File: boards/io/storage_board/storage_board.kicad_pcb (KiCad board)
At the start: 2 copper layers, 40.6 x 20.3 mm, 17 parts, among them J1 Conn_02x06_Top_Bottom, J2 Conn_02x02_Odd_Even, Q1 2SC3325, Q2 2SC3325, Q3 2SC3325, Q4 2SC3325, U1 24FC512

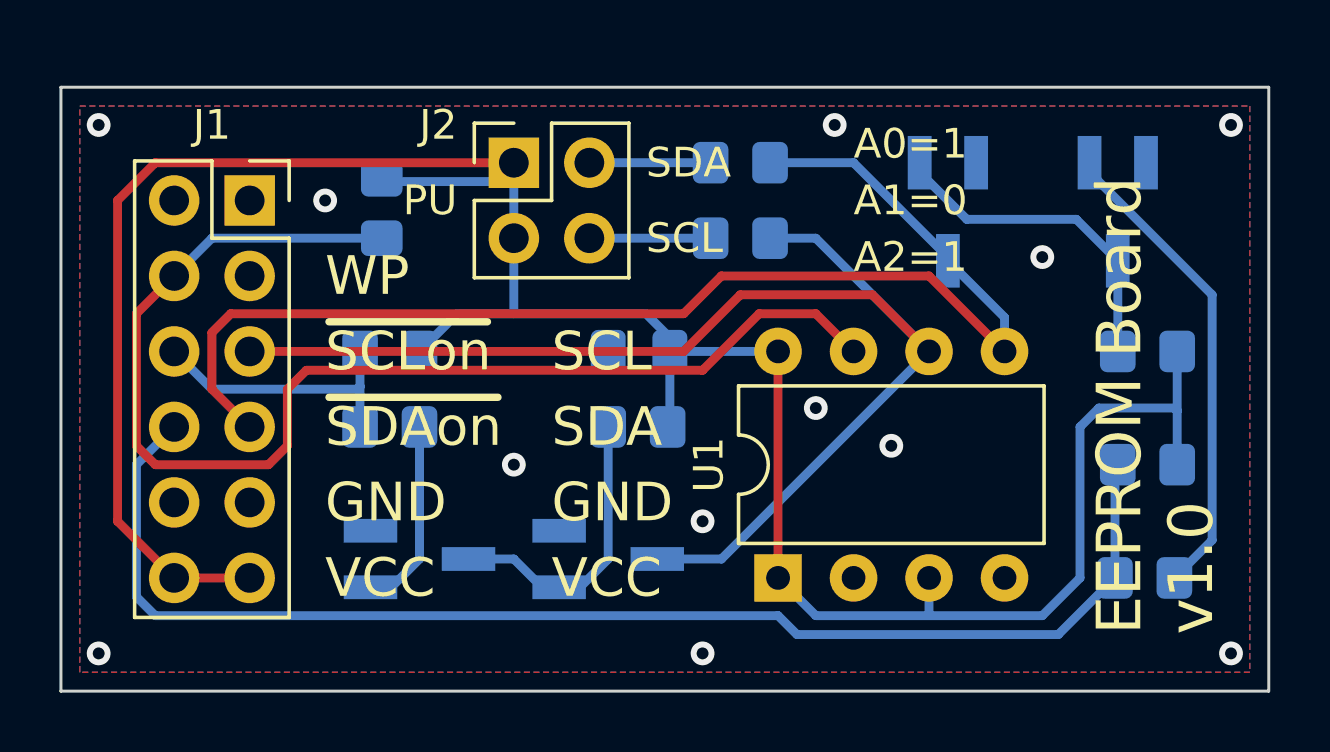
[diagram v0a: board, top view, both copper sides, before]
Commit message: storage_board: rename and improve line width
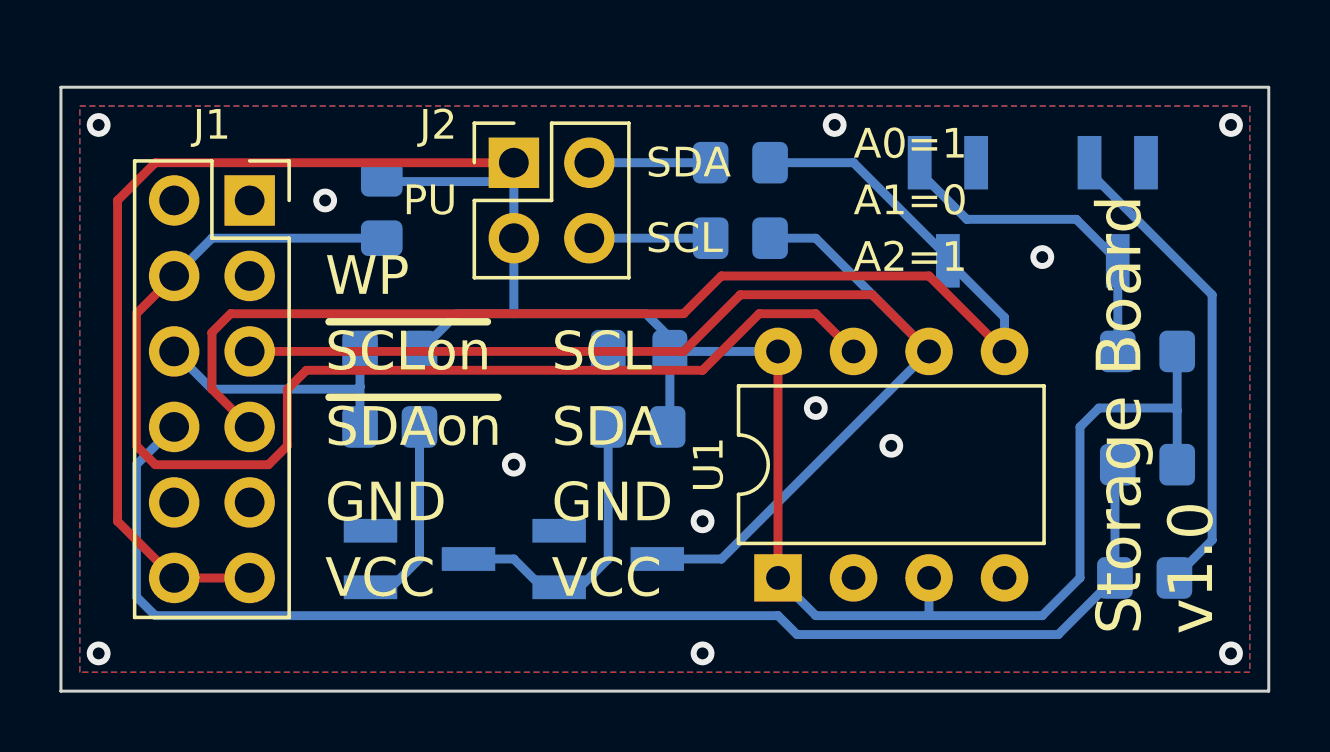
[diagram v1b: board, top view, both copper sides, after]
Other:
- board text added: "Storage Board v1.0"
- board text removed: "EEPROM Board v1.0"

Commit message: release boards
* rom_adapter_for_nucky
* software_rom2
* eprom_zps
* convenient_port_shield
* storage_board
* timer_board
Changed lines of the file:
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@@
     (aux_axis_origin 85.09 87.63)
     (pcbplotparams
-      (layerselection 0x00010fc_ffffffff)
+      (layerselection 0x00010f0_ffffffff)
       (disableapertmacros false)
       (usegerberextensions false)
@@
       (viasonmask false)
       (mode 1)
-      (useauxorigin false)
+      (useauxorigin true)
       (hpglpennumber 1)
       (hpglpenspeed 20)
@@
       (outputformat 1)
       (mirror false)
-      (drillshape 1)
+      (drillshape 0)
       (scaleselection 1)
-      (outputdirectory "")
+      (outputdirectory "../../../../release/20220527-boards-v1.0/_gerver_work/storage_board/")
     )
   )
@@
     (fp_line (start -1 -0.625) (end -1 0.625) (layer "B.Fab") (width 0.1))
     (fp_line (start -1 0.625) (end 1 0.625) (layer "B.Fab") (width 0.1))
-    (pad "1" smd roundrect (at -1 0) (size 1.2 1.4) (layers "B.Cu" "B.Paste" "B.Mask") (roundrect_rratio 0.208333)
+    (pad "1" smd roundrect (at -1 0) (size 1.2 1.4) (layers "B.Cu" "B.Paste" "B.Mask") (roundrect_rratio 0.2083333333)
       (net 9 "/~{SCL_DRV}") (pintype "passive"))
-    (pad "2" smd roundrect (at 1 0) (size 1.2 1.4) (layers "B.Cu" "B.Paste" "B.Mask") (roundrect_rratio 0.208333)
+    (pad "2" smd roundrect (at 1 0) (size 1.2 1.4) (layers "B.Cu" "B.Paste" "B.Mask") (roundrect_rratio 0.2083333333)
       (net 15 "Net-(Q3-Pad1)") (pintype "passive"))
     (model "${KICAD6_3DMODEL_DIR}/Resistor_SMD.3dshapes/R_0805_2012Metric.wrl"
@@
     (fp_line (start 1 0.625) (end 1 -0.625) (layer "B.Fab") (width 0.1))
     (fp_line (start -1 0.625) (end 1 0.625) (layer "B.Fab") (width 0.1))
-    (pad "1" smd roundrect (at -1 0 90) (size 1.2 1.4) (layers "B.Cu" "B.Paste" "B.Mask") (roundrect_rratio 0.208333)
+    (pad "1" smd roundrect (at -1 0 90) (size 1.2 1.4) (layers "B.Cu" "B.Paste" "B.Mask") (roundrect_rratio 0.2083333333)
       (net 8 "/WP") (pintype "passive"))
-    (pad "2" smd roundrect (at 1 0 90) (size 1.2 1.4) (layers "B.Cu" "B.Paste" "B.Mask") (roundrect_rratio 0.208333)
+    (pad "2" smd roundrect (at 1 0 90) (size 1.2 1.4) (layers "B.Cu" "B.Paste" "B.Mask") (roundrect_rratio 0.2083333333)
       (net 1 "VCC") (pintype "passive"))
     (model "${KICAD6_3DMODEL_DIR}/Resistor_SMD.3dshapes/R_0805_2012Metric.wrl"
@@
     (fp_line (start -1 -0.625) (end -1 0.625) (layer "B.Fab") (width 0.1))
     (fp_line (start -1 0.625) (end 1 0.625) (layer "B.Fab") (width 0.1))
-    (pad "1" smd roundrect (at -1 0) (size 1.2 1.4) (layers "B.Cu" "B.Paste" "B.Mask") (roundrect_rratio 0.208333)
+    (pad "1" smd roundrect (at -1 0) (size 1.2 1.4) (layers "B.Cu" "B.Paste" "B.Mask") (roundrect_rratio 0.2083333333)
       (net 14 "Net-(Q1-Pad3)") (pintype "passive"))
-    (pad "2" smd roundrect (at 1 0) (size 1.2 1.4) (layers "B.Cu" "B.Paste" "B.Mask") (roundrect_rratio 0.208333)
+    (pad "2" smd roundrect (at 1 0) (size 1.2 1.4) (layers "B.Cu" "B.Paste" "B.Mask") (roundrect_rratio 0.2083333333)
       (net 1 "VCC") (pintype "passive"))
     (model "${KICAD6_3DMODEL_DIR}/Resistor_SMD.3dshapes/R_0805_2012Metric.wrl"
@@
     (fp_line (start -1 -0.625) (end -1 0.625) (layer "B.Fab") (width 0.1))
     (fp_line (start 1 0.625) (end 1 -0.625) (layer "B.Fab") (width 0.1))
-    (pad "1" smd roundrect (at -1 0) (size 1.2 1.4) (layers "B.Cu" "B.Paste" "B.Mask") (roundrect_rratio 0.208333)
+    (pad "1" smd roundrect (at -1 0) (size 1.2 1.4) (layers "B.Cu" "B.Paste" "B.Mask") (roundrect_rratio 0.2083333333)
       (net 10 "/~{SDA_DRV}") (pintype "passive"))
-    (pad "2" smd roundrect (at 1 0) (size 1.2 1.4) (layers "B.Cu" "B.Paste" "B.Mask") (roundrect_rratio 0.208333)
+    (pad "2" smd roundrect (at 1 0) (size 1.2 1.4) (layers "B.Cu" "B.Paste" "B.Mask") (roundrect_rratio 0.2083333333)
       (net 13 "Net-(Q1-Pad1)") (pintype "passive"))
     (model "${KICAD6_3DMODEL_DIR}/Resistor_SMD.3dshapes/R_0805_2012Metric.wrl"
@@
     (fp_line (start -1 0.625) (end 1 0.625) (layer "B.Fab") (width 0.1))
     (fp_line (start 1 -0.625) (end -1 -0.625) (layer "B.Fab") (width 0.1))
-    (pad "1" smd roundrect (at -1 0) (size 1.2 1.4) (layers "B.Cu" "B.Paste" "B.Mask") (roundrect_rratio 0.208333)
+    (pad "1" smd roundrect (at -1 0) (size 1.2 1.4) (layers "B.Cu" "B.Paste" "B.Mask") (roundrect_rratio 0.2083333333)
       (net 9 "/~{SCL_DRV}") (pintype "passive"))
-    (pad "2" smd roundrect (at 1 0) (size 1.2 1.4) (layers "B.Cu" "B.Paste" "B.Mask") (roundrect_rratio 0.208333)
+    (pad "2" smd roundrect (at 1 0) (size 1.2 1.4) (layers "B.Cu" "B.Paste" "B.Mask") (roundrect_rratio 0.2083333333)
       (net 1 "VCC") (pintype "passive"))
     (model "${KICAD6_3DMODEL_DIR}/Resistor_SMD.3dshapes/R_0805_2012Metric.wrl"
@@
     (fp_line (start 1 0.625) (end 1 -0.625) (layer "B.Fab") (width 0.1))
     (fp_line (start -1 0.625) (end 1 0.625) (layer "B.Fab") (width 0.1))
-    (pad "1" smd roundrect (at -1 0 180) (size 1.2 1.4) (layers "B.Cu" "B.Paste" "B.Mask") (roundrect_rratio 0.208333)
+    (pad "1" smd roundrect (at -1 0 180) (size 1.2 1.4) (layers "B.Cu" "B.Paste" "B.Mask") (roundrect_rratio 0.2083333333)
       (net 6 "/SDA") (pintype "passive"))
-    (pad "2" smd roundrect (at 1 0 180) (size 1.2 1.4) (layers "B.Cu" "B.Paste" "B.Mask") (roundrect_rratio 0.208333)
+    (pad "2" smd roundrect (at 1 0 180) (size 1.2 1.4) (layers "B.Cu" "B.Paste" "B.Mask") (roundrect_rratio 0.2083333333)
       (net 11 "/SDA_PU") (pintype "passive"))
     (model "${KICAD6_3DMODEL_DIR}/Resistor_SMD.3dshapes/R_0805_2012Metric.wrl"
@@
     (fp_line (start -1 -0.625) (end -1 0.625) (layer "B.Fab") (width 0.1))
     (fp_line (start -1 0.625) (end 1 0.625) (layer "B.Fab") (width 0.1))
-    (pad "1" smd roundrect (at -1 0) (size 1.2 1.4) (layers "B.Cu" "B.Paste" "B.Mask") (roundrect_rratio 0.208333)
+    (pad "1" smd roundrect (at -1 0) (size 1.2 1.4) (layers "B.Cu" "B.Paste" "B.Mask") (roundrect_rratio 0.2083333333)
       (net 10 "/~{SDA_DRV}") (pintype "passive"))
-    (pad "2" smd roundrect (at 1 0) (size 1.2 1.4) (layers "B.Cu" "B.Paste" "B.Mask") (roundrect_rratio 0.208333)
+    (pad "2" smd roundrect (at 1 0) (size 1.2 1.4) (layers "B.Cu" "B.Paste" "B.Mask") (roundrect_rratio 0.2083333333)
       (net 1 "VCC") (pintype "passive"))
     (model "${KICAD6_3DMODEL_DIR}/Resistor_SMD.3dshapes/R_0805_2012Metric.wrl"
@@
     (fp_line (start -1 0.625) (end 1 0.625) (layer "B.Fab") (width 0.1))
     (fp_line (start -1 -0.625) (end -1 0.625) (layer "B.Fab") (width 0.1))
-    (pad "1" smd roundrect (at -1.0375 0 180) (size 1.175 1.45) (layers "B.Cu" "B.Paste" "B.Mask") (roundrect_rratio 0.212766)
+    (pad "1" smd roundrect (at -1.0375 0 180) (size 1.175 1.45) (layers "B.Cu" "B.Paste" "B.Mask") (roundrect_rratio 0.2127659574)
       (net 1 "VCC") (pintype "passive"))
-    (pad "2" smd roundrect (at 1.0375 0 180) (size 1.175 1.45) (layers "B.Cu" "B.Paste" "B.Mask") (roundrect_rratio 0.212766)
+    (pad "2" smd roundrect (at 1.0375 0 180) (size 1.175 1.45) (layers "B.Cu" "B.Paste" "B.Mask") (roundrect_rratio 0.2127659574)
       (net 2 "GND") (pintype "passive"))
     (model "${KICAD6_3DMODEL_DIR}/Capacitor_SMD.3dshapes/C_0805_2012Metric.wrl"
@@
     (fp_line (start 1 0.625) (end 1 -0.625) (layer "B.Fab") (width 0.1))
     (fp_line (start 1 -0.625) (end -1 -0.625) (layer "B.Fab") (width 0.1))
-    (pad "1" smd roundrect (at -1 0) (size 1.2 1.4) (layers "B.Cu" "B.Paste" "B.Mask") (roundrect_rratio 0.208333)
+    (pad "1" smd roundrect (at -1 0) (size 1.2 1.4) (layers "B.Cu" "B.Paste" "B.Mask") (roundrect_rratio 0.2083333333)
       (net 16 "Net-(Q3-Pad3)") (pintype "passive"))
-    (pad "2" smd roundrect (at 1 0) (size 1.2 1.4) (layers "B.Cu" "B.Paste" "B.Mask") (roundrect_rratio 0.208333)
+    (pad "2" smd roundrect (at 1 0) (size 1.2 1.4) (layers "B.Cu" "B.Paste" "B.Mask") (roundrect_rratio 0.2083333333)
       (net 1 "VCC") (pintype "passive"))
     (model "${KICAD6_3DMODEL_DIR}/Resistor_SMD.3dshapes/R_0805_2012Metric.wrl"
@@
     (fp_line (start 1 0.625) (end 1 -0.625) (layer "B.Fab") (width 0.1))
     (fp_line (start -1 -0.625) (end -1 0.625) (layer "B.Fab") (width 0.1))
-    (pad "1" smd roundrect (at -1 0 180) (size 1.2 1.4) (layers "B.Cu" "B.Paste" "B.Mask") (roundrect_rratio 0.208333)
+    (pad "1" smd roundrect (at -1 0 180) (size 1.2 1.4) (layers "B.Cu" "B.Paste" "B.Mask") (roundrect_rratio 0.2083333333)
       (net 5 "/SCL") (pintype "passive"))
-    (pad "2" smd roundrect (at 1 0 180) (size 1.2 1.4) (layers "B.Cu" "B.Paste" "B.Mask") (roundrect_rratio 0.208333)
+    (pad "2" smd roundrect (at 1 0 180) (size 1.2 1.4) (layers "B.Cu" "B.Paste" "B.Mask") (roundrect_rratio 0.2083333333)
       (net 12 "/SCL_PU") (pintype "passive"))
     (model "${KICAD6_3DMODEL_DIR}/Resistor_SMD.3dshapes/R_0805_2012Metric.wrl"
